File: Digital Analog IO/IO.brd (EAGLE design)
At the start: 61.3 x 30.5 mm, 24 parts, among them IC1 LD117AS33TR

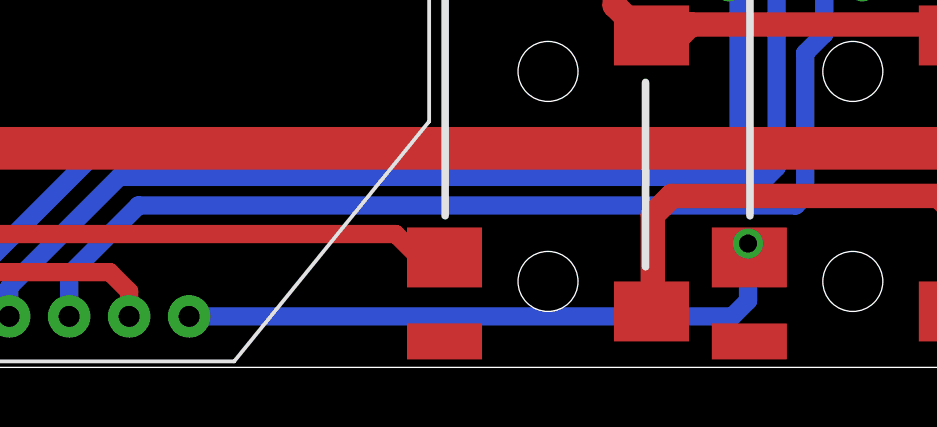
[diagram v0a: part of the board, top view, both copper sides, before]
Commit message: Electric current module
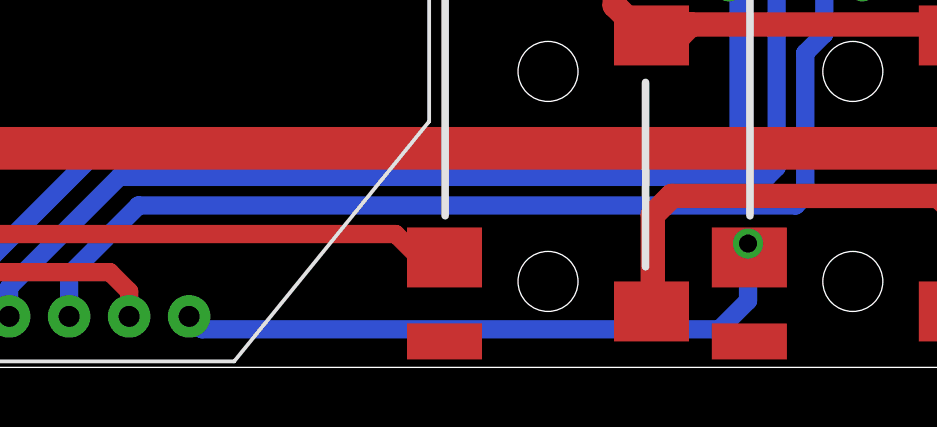
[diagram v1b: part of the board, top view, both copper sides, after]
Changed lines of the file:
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@@
 <contactref element="OPENMOTE" pad="20"/>
 <via x="39.0525" y="4.1275" extent="1-16" drill="0.6"/>
-<wire x1="20.4225" y1="1.7" x2="38.53" y2="1.7" width="0.6096" layer="16"/>
-<wire x1="38.53" y1="1.7" x2="39.0525" y2="2.2225" width="0.6096" layer="16"/>
+<wire x1="38.1" y1="1.27" x2="39.0525" y2="2.2225" width="0.6096" layer="16"/>
 <wire x1="39.0525" y1="4.1275" x2="39.0525" y2="3.7075" width="0.6096" layer="1"/>
 <wire x1="39.0525" y1="3.7075" x2="39.095" y2="3.665" width="0.6096" layer="1"/>
 <wire x1="39.0525" y1="2.2225" x2="39.0525" y2="4.1275" width="0.6096" layer="16"/>
+<wire x1="38.1" y1="1.27" x2="20.8525" y2="1.27" width="0.6096" layer="16"/>
+<wire x1="20.8525" y1="1.27" x2="20.4225" y2="1.7" width="0.6096" layer="16"/>
 </signal>
 <signal name="AN-IN-4-20MA-1">
